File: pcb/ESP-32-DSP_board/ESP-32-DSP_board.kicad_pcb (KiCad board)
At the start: 4 copper layers, 58.2 x 74.6 mm, 71 parts, among them J1 USB_C_Receptacle_USB2.0, J12 Conn_Coaxial, J2 Conn_01x10_Pin, J3 AudioJack2_Ground, J4 Conn_01x08_Pin, J5 SD_Card, J6 Conn_01x08_Pin, J7 Conn_01x08_Pin, SW1 Reset, SW2 Boot, U1 AZ1117IH-3.3, U2 AD5689BRUZ, U3 USBLC6-2P6, U4 LM386, U5 ADS8688, U6 ESP32-S3FH4R2, Y1 40MHz

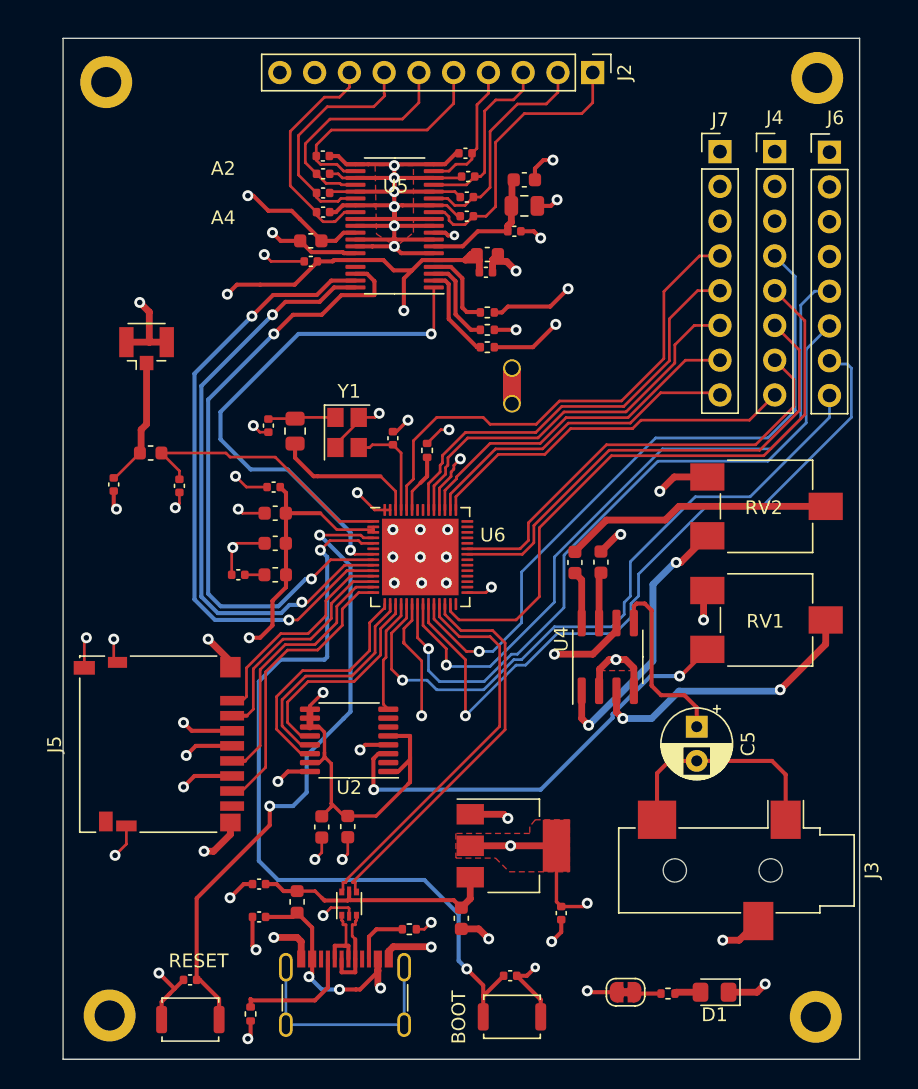
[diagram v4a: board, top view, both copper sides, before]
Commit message: ESP32-S3 DSP updates
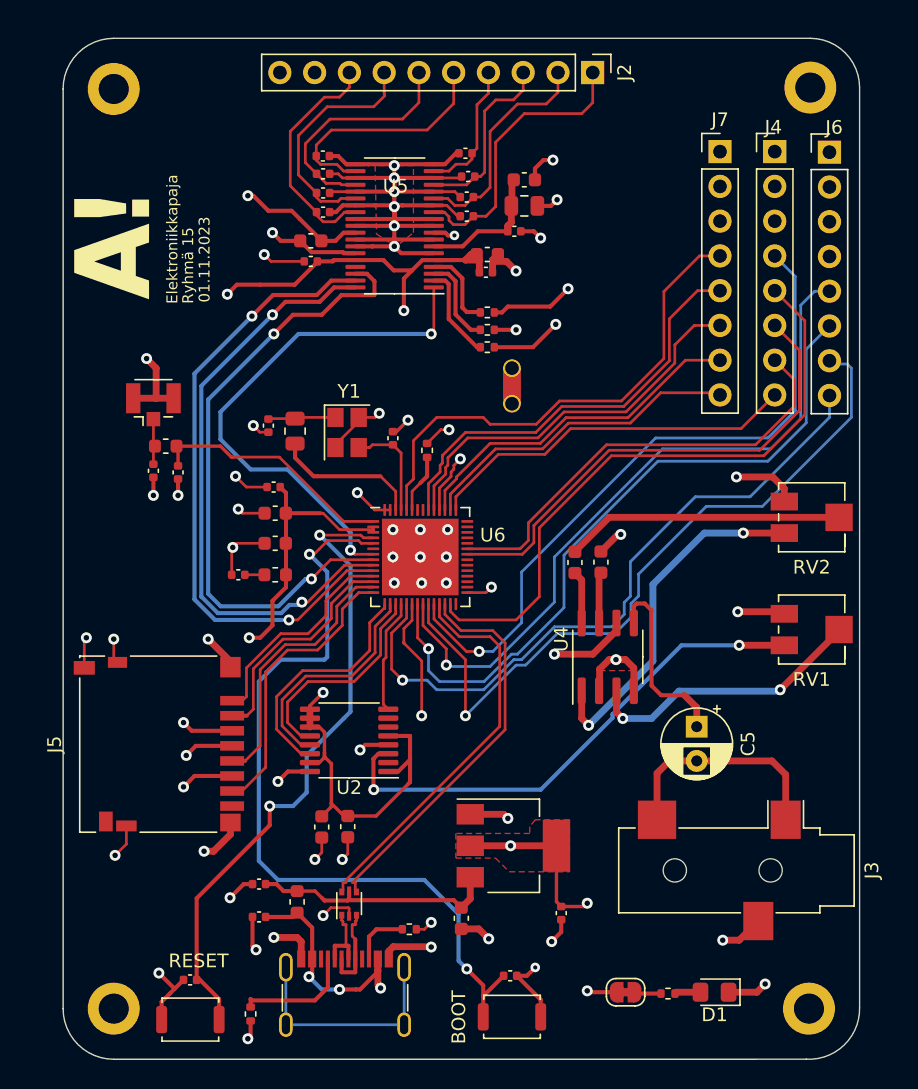
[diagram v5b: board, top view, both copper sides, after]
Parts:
- added G***: LOGO, LOGO, F.Cu at (104.6, 77.7)
- RV1, RV2: value R_Potentiometer -> 10k; footprint Potentiometer_SMD:Potentiometer_ACP_CA6-VSMD_Vertical -> Potentiometer_SMD:Potentiometer_Bourns_3214J_Horizontal
- moved J12 4.13 mm to (107.7, 89.6)
- moved RV2 3.40 mm to (155.8, 97.8), turned to 180 degrees
- moved RV1 3.37 mm to (155.8, 106.0), turned to 180 degrees
- moved C28 3.07 mm to (107.7, 94.4)
- moved L1 1.21 mm to (108.6, 92.6)
- moved C27 0.99 mm to (109.5, 94.5)
- moved H1 0.86 mm to (155.7, 66.4)
- moved H4 0.78 mm to (155.6, 133.7)
- moved H2 0.74 mm to (104.8, 66.5)
- moved H3 0.58 mm to (104.8, 133.7)
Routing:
- net Net-(J12-In): track 9.32 -> 3.39 mm
- net Net-(U2-VOUTA): track 32.3 -> 38.0 mm
- net Net-(RV2-Pad1): track 20.4 -> 26.1 mm
- net GNDA: track 158.6 -> 162.8 mm
- net Net-(U6-LNA_IN/RF): track 20.0 -> 18.1 mm
- net /IO0: track 57.7 -> 58.6 mm
- net Net-(C7-Pad2): track 19.7 -> 20.4 mm
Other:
- outline, holes or cut-outs redrawn
- board text added: "01.11.2023"
- board text added: "Elektroniikkapaja"
- board text added: "Ryhmä 15"
- board text removed: "A2"
- board text removed: "A4"

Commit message: Fixed mistake in S3 dsp
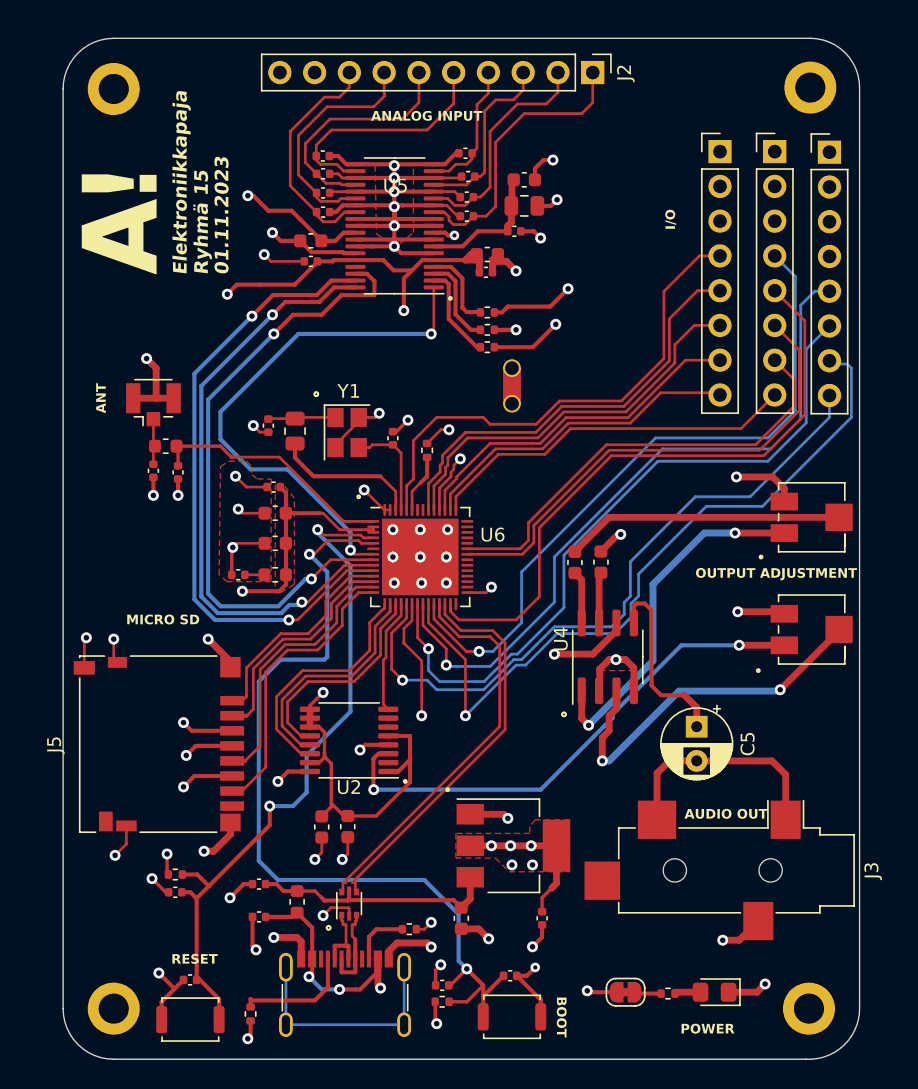
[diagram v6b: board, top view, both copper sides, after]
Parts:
- added C11: 100n, Capacitor_SMD:C_0402_1005Metric, F.Cu at (109.3, 125.2)
- added C35: 100n, Capacitor_SMD:C_0402_1005Metric, F.Cu at (128.8, 132.0)
- added R1: 10k, Resistor_SMD:R_0402_1005Metric, F.Cu at (109.3, 123.9)
- added R2: 10k, Resistor_SMD:R_0402_1005Metric, F.Cu at (128.8, 133.2)
- J3: footprint Connector_Audio:Jack_3.5mm_CUI_SJ-3523-SMT_Horizontal -> Connector_Audio:Jack_3.5mm_CUI_SJ-3524-SMT_Horizontal
- moved G*** 1.89 mm to (105.2, 75.9)
- moved C1 1.45 mm to (136.1, 127.1)
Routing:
- net Net-(U4-+): track 20.8 -> 26.9 mm
- net /IO0: track 58.6 -> 63.4 mm
- net /EN: track 46.8 -> 51.1 mm
- net GND: track 104.5 -> 108.0 mm, vias 45 -> 47
- net +5V: track 183.9 -> 184.6 mm
- net +3.3V: track 136.1 -> 136.0 mm, vias 17 -> 22
- added copper zone on F.Cu, net GND
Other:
- board text added: "ANALOG INPUT"
- board text added: "ANT"
- board text added: "AUDIO OUT"
- board text added: "I/O"
- board text added: "MICRO SD"
- board text added: "OUTPUT ADJUSTMENT"
- board text added: "POWER"
- board text removed: "J6"

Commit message: ESP32-S3 DSP board
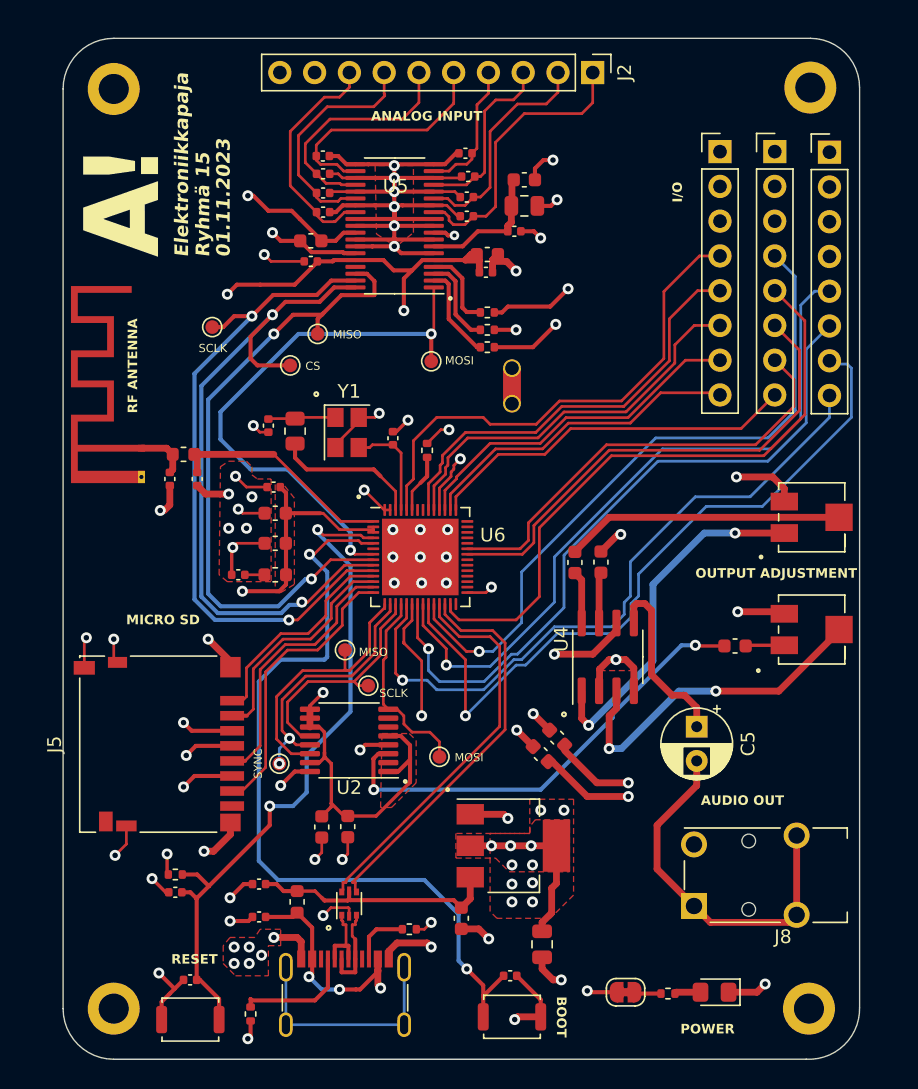
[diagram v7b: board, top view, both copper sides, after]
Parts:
- removed C35: 100n, Capacitor_SMD:C_0402_1005Metric
- removed J3: AudioJack2_Ground, Connector_Audio:Jack_3.5mm_CUI_SJ-3524-SMT_Horizontal
- removed R2: 10k, Resistor_SMD:R_0402_1005Metric
- added C37: 100n, Capacitor_SMD:C_0603_1608Metric, F.Cu at (137.2, 113.9)
- added C38: 10u, Capacitor_SMD:C_0603_1608Metric, F.Cu at (136.0, 115.1)
- added C39: 10u, Capacitor_SMD:C_0603_1608Metric, F.Cu at (150.2, 107.2)
- added J8: AudioJack3, Connector_Audio:Jack_3.5mm_Switronic_ST-005-G_horizontal, F.Cu at (153.7, 124.0)
- added TP1: TestPoint, TestPoint:TestPoint_Pad_D1.0mm, F.Cu at (119.7, 84.4)
- added TP2: TestPoint, TestPoint:TestPoint_Pad_D1.0mm, F.Cu at (117.7, 86.7)
- added TP3: TestPoint, TestPoint:TestPoint_Pad_D1.0mm, F.Cu at (112.0, 83.9)
- added TP4: TestPoint, TestPoint:TestPoint_Pad_D1.0mm, F.Cu at (128.6, 115.3)
- added TP5: TestPoint, TestPoint:TestPoint_Pad_D1.0mm, F.Cu at (128.0, 86.4)
- added TP6: TestPoint, TestPoint:TestPoint_Pad_D1.0mm, F.Cu at (123.4, 110.1)
- added TP7: TestPoint, TestPoint:TestPoint_Pad_D1.0mm, F.Cu at (116.9, 115.8)
- added TP8: TestPoint, TestPoint:TestPoint_Pad_D1.0mm, F.Cu at (121.7, 107.5)
- C1: footprint Capacitor_SMD:C_0402_1005Metric -> Capacitor_SMD:C_0805_2012Metric
- J12: footprint Connector_Coaxial:U.FL_Hirose_U.FL-R-SMT-1_Vertical -> RF_Antenna:Texas_SWRA117D_2.4GHz_Right
- moved J12 3.29 mm to (106.8, 92.8)
- moved C1 1.90 mm to (136.1, 129.0)
- moved C27 1.48 mm to (110.9, 95.0)
- moved L1 1.43 mm to (109.9, 93.2)
- moved C28 1.34 mm to (108.9, 95.0)
- moved G*** 1.30 mm to (105.3, 74.6)
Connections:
- RV1 pad 1: Net-(U2-VOUTA) -> Net-(C39-Pad2)
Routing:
- net +5V: track 184.6 -> 220.7 mm, vias 4 -> 6
- net Net-(C5-Pad2): track 16.9 -> 26.9 mm
- net /ADC_CS: track 44.1 -> 51.1 mm
- net /DAC_MOSI: track 8.29 -> 14.5 mm
- net GND: track 108.0 -> 102.8 mm, vias 47 -> 53
- net /IO0: track 63.4 -> 58.6 mm
- net Net-(U2-VOUTA): track 38.0 -> 33.7 mm
- net /ADC_SCLK: track 46.3 -> 49.5 mm
- net Net-(C39-Pad2): track 0.00 -> 2.85 mm
- net GNDA: track 162.8 -> 165.3 mm, vias 15 -> 16
- net /DAC_SYNC: track 16.8 -> 19.1 mm, vias 0 -> 2
- net /ADC_MOSI: track 38.4 -> 40.4 mm
- net Net-(U4-+): track 26.9 -> 24.9 mm
- net /DAC_MISO: track 17.6 -> 19.6 mm
- net /ADC_MISO: track 46.0 -> 47.6 mm
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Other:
- board text added: "CS"
- board text added: "MISO"
- board text added: "MOSI"
- board text added: "RF ANTENNA"
- board text added: "SCLK"
- board text added: "SYNC"
- board text removed: "ANT"

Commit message: Added local pcb modifications
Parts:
- C37, C9: footprint Capacitor_SMD:C_0603_1608Metric -> Capacitor_SMD:C_0402_1005Metric
- J8: footprint Connector_Audio:Jack_3.5mm_Switronic_ST-005-G_horizontal -> Connector_Audio:Jack_3.5mm_CUI_SJ-3523-SMT_Horizontal
- moved J8 3.10 mm to (150.6, 123.8), turned to -90 degrees
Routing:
- net Net-(C5-Pad2): track 26.9 -> 20.0 mm
- net GNDA: track 165.3 -> 163.5 mm, vias 16 -> 17
- net GND: track 102.8 -> 104.2 mm
- net +3.3V: track 135.4 -> 136.1 mm
